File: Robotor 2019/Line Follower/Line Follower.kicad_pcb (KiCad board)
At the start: 2 copper layers, 3.7 x 3.6 mm, 96 parts, among them J1 Conn_01x03_Male, J2 Conn_01x04_Female, J3 USB_B_Mini, J4 Conn_01x03_Female, J5 Conn_01x03_Female, J7 Conn_01x03_Female, J8 Conn_01x03_Female, M1 Motor_DC, M2 Motor_DC, U1 AMS1117-3V3, U10 ITR8307, U11 ITR8307, U12 ITR8307, U13 ITR8307, U14 ITR8307, U15 ITR8307, U3 AMS1117-5.0, U4 STM32F103C8Tx, U5 ITR8307, U6 L298P, U7 ITR8307, U8 ITR8307, U9 ITR8307, Y1 32.768Khz, Y2 8Mhz

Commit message: Line Follower robot electric schematic and PCB.
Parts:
- added REF**: MountingHole_2.5mm, MountingHole:MountingHole_2.5mm, B.Cu at (55.6, 42.0)
- added REF**: MountingHole_2.5mm, MountingHole:MountingHole_2.5mm, B.Cu at (40.6, 42.2)
- added REF**: MountingHole_2.5mm, MountingHole:MountingHole_2.5mm, F.Cu at (55.6, 168.8)
- added REF**: MountingHole_2.5mm, MountingHole:MountingHole_2.5mm, F.Cu at (40.6, 168.7)
- added REF**: MountingHole_2.5mm, MountingHole:MountingHole_2.5mm, F.Cu at (248.9, 46.0)
- added REF**: MountingHole_2.5mm, MountingHole:MountingHole_2.5mm, F.Cu at (224.5, 46.0)
- added REF**: MountingHole_2.5mm, MountingHole:MountingHole_2.5mm, B.Cu at (248.9, 164.8)
- added REF**: MountingHole_2.5mm, MountingHole:MountingHole_2.5mm, B.Cu at (224.5, 164.8)
- added SW1: SW_Push, Button_Switch_SMD:SW_Push_1P1T_NO_6x6mm_H9.5mm, F.Cu at (117.0, 122.3)
- C15, C16, C17, C18, C19, C20, C21, C22, C23, C24, J3, R10, R11, R12, R14, R16, R18, R22, R24, R26, R28, R3, R30, R32, R9, U10, U11, U12, U13, U14, U15, U5, U7, U8, U9: moved to B.Cu
- R13, R15, R17, R19, R21, R23, R25, R27, R29, R31: footprint Resistor_SMD:R_0805_2012Metric_Pad1.15x1.40mm_HandSolder -> Resistor_SMD:R_1206_3216Metric_Pad1.42x1.75mm_HandSolder; moved to B.Cu
- moved J7 229.0 mm to (254.0, 146.1)
- moved J3 224.8 mm to (256.0, 104.4), turned to 270 degrees
- moved J8 210.1 mm to (221.7, 146.9)
- moved J1 194.1 mm to (157.0, 163.3), turned to 270 degrees
- moved D7 190.2 mm to (187.7, 172.0), turned to 180 degrees
- moved J4 187.0 mm to (254.0, 66.5), turned to 180 degrees
- moved R5 184.4 mm to (255.0, 137.7), turned to 180 degrees
- moved R10 182.2 mm to (242.1, 103.9), turned to 90 degrees
- moved D8 179.1 mm to (182.6, 165.1)
- moved M2 177.2 mm to (183.9, 149.1), turned to 270 degrees
- moved R33 176.9 mm to (256.0, 54.6)
- moved D5 171.7 mm to (168.7, 171.2)
- moved D6 171.5 mm to (173.7, 165.1), turned to 180 degrees
- moved R9 171.3 mm to (244.9, 97.5), turned to 180 degrees
- moved U1 169.4 mm to (133.3, 185.8), turned to 180 degrees
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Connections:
- net US3_IN renamed Net-(U4-Pad45)
- net US3_OUT renamed Net-(U4-Pad46)
- C15 pad 1: +5V -> +3V3
- C16 pad 1: +5V -> +3V3
- C17 pad 1: +5V -> +3V3
- C18 pad 1: +5V -> +3V3
- C19 pad 1: +5V -> +3V3
- C20 pad 1: +5V -> +3V3
- C21 pad 1: +5V -> +3V3
- C22 pad 1: +5V -> +3V3
- C23 pad 1: +5V -> +3V3
- C24 pad 1: +5V -> +3V3
- R12 pad 1: +5V -> +3V3
- R13 pad 1: S7 -> S1
- R14 pad 1: +5V -> +3V3
- R15 pad 1: S8 -> S2
- R16 pad 1: +5V -> +3V3
- R17 pad 1: S9 -> S3
- R18 pad 1: +5V -> +3V3
- R19 pad 1: S10 -> S4
- R21 pad 1: S6 -> S8
- R22 pad 1: +5V -> +3V3
- R23 pad 1: S5 -> S7
- R24 pad 1: +5V -> +3V3
- R25 pad 1: S4 -> S6
- R26 pad 1: +5V -> +3V3
- R27 pad 1: S3 -> S5
- R28 pad 1: +5V -> +3V3
- R29 pad 1: S2 -> S10
- R30 pad 1: +5V -> +3V3
- R31 pad 1: S1 -> S9
- R32 pad 1: +5V -> +3V3
- U4 pad 10: S1 -> S3
- U4 pad 12: S3 -> S1
- U4 pad 14: S5 -> S8
- U4 pad 15: S6 -> S7
- U4 pad 16: S7 -> S6
- U4 pad 17: S8 -> S5
- U4 pad 18: S9 -> S10
- U4 pad 19: S10 -> S9
- U4 pad 21: H4 -> Net-(U4-Pad21)
- U4 pad 22: H3 -> Net-(U4-Pad22)
- U4 pad 25: US1_IN -> H1
- U4 pad 26: US1_OUT -> H2
- U4 pad 27: US2_IN -> H3
- U4 pad 28: US2_OUT -> H4
- U4 pad 30: EnA -> Net-(U4-Pad30)
- U4 pad 31: EnB -> Net-(U4-Pad31)
- U4 pad 39: M2IN1 -> EnB
- U4 pad 40: M1IN2 -> M2IN1
- U4 pad 41: M1IN1 -> EnA
- U4 pad 42: H2 -> M1IN2
- U4 pad 43: H1 -> M1IN1
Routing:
- net +3V3: track 0.00 -> 1078.7 mm, vias 0 -> 2
- net +7.5V: track 0.00 -> 471.6 mm
- net +5V: track 0.00 -> 286.5 mm
- net Net-(D3-Pad2): track 0.00 -> 189.9 mm
- net Net-(D1-Pad2): track 0.00 -> 185.8 mm
- net S9: track 0.00 -> 177.2 mm, vias 0 -> 1
- net S10: track 0.00 -> 166.5 mm, vias 0 -> 1
- net H3: track 0.00 -> 154.8 mm, vias 0 -> 1
- net S1: track 0.00 -> 153.0 mm, vias 0 -> 1
- net S5: track 0.00 -> 152.8 mm, vias 0 -> 1
- net H2: track 0.00 -> 150.0 mm, vias 0 -> 1
- net Net-(D5-Pad2): track 0.00 -> 148.5 mm
- net S2: track 0.00 -> 140.6 mm, vias 0 -> 1
- net Net-(D7-Pad2): track 0.00 -> 140.4 mm
- net S6: track 0.00 -> 135.7 mm, vias 0 -> 1
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- added copper zone on B.Cu, net GND
- added copper zone on F.Cu, net GND
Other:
- board size 3.7 x 3.6 mm -> 239.3 x 180.3 mm

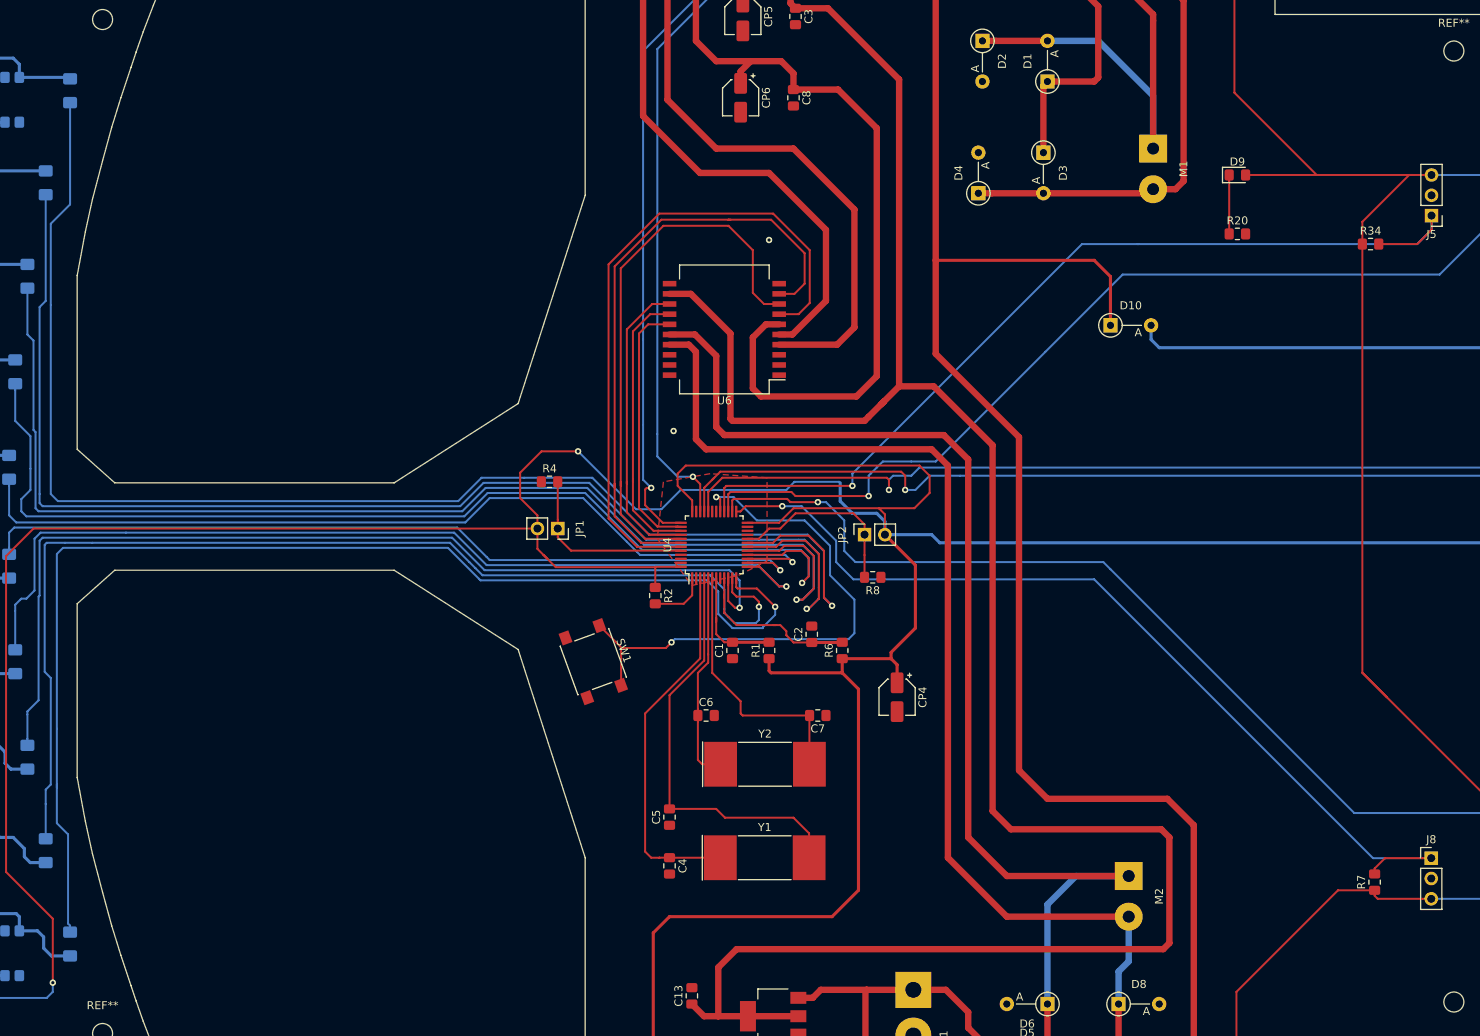
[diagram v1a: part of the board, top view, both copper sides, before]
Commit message: Small tweaks to vias, paths, added parts lists.
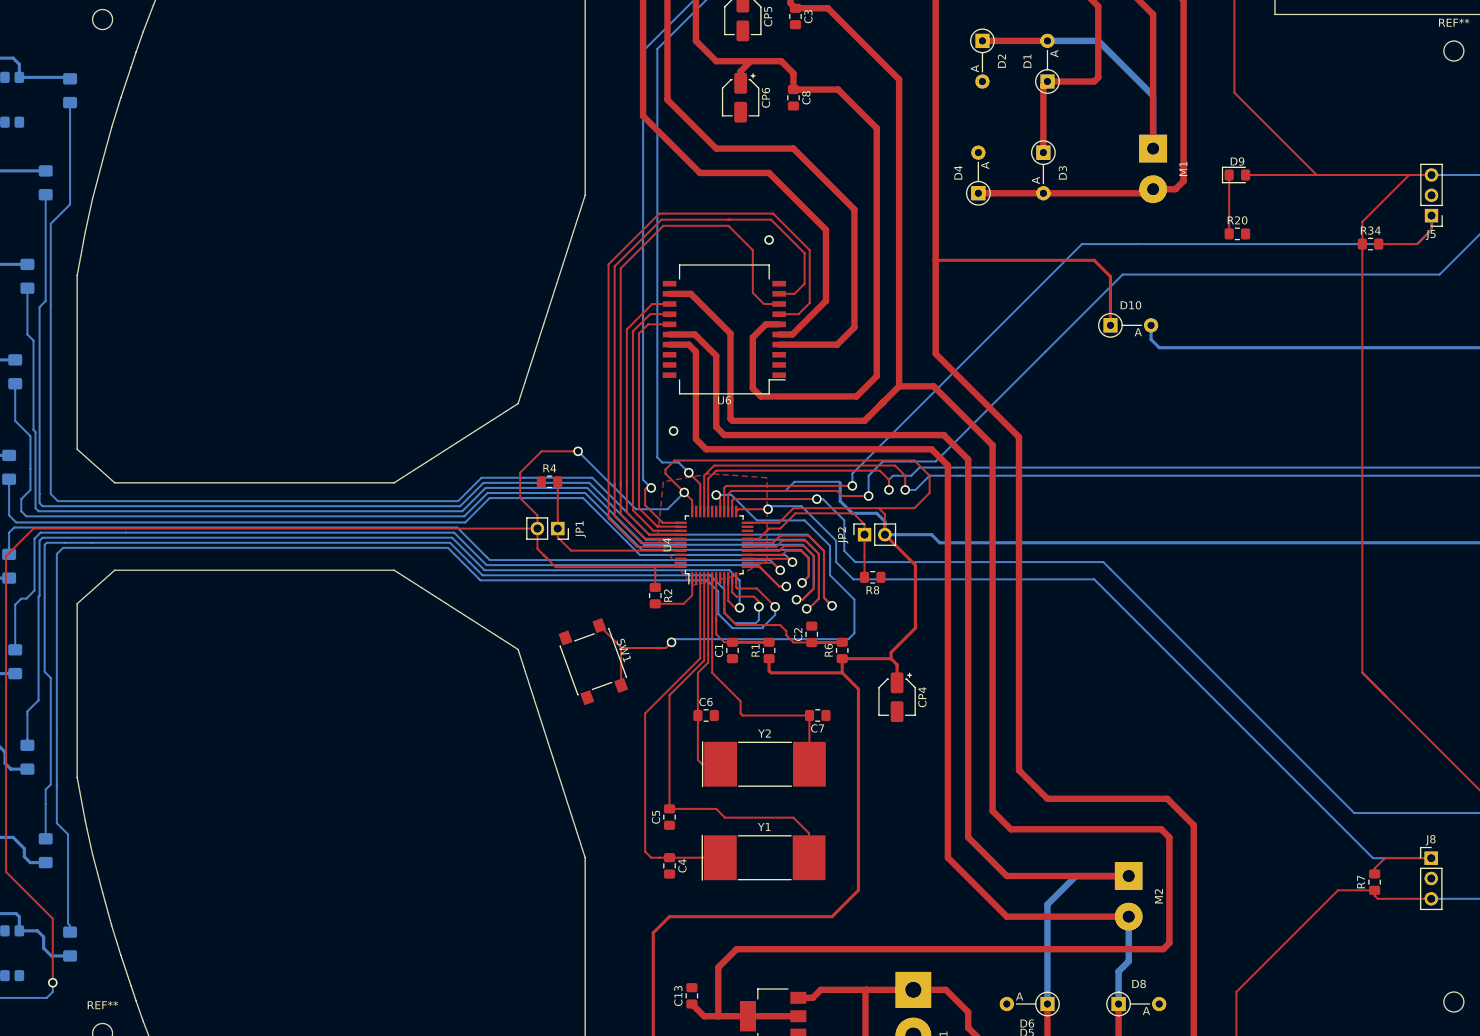
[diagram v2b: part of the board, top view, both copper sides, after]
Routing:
- net +3V3: track 1078.7 -> 1068.7 mm, vias 2 -> 3
- net PA11: track 119.2 -> 120.9 mm
- net PA12: track 120.5 -> 121.7 mm

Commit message: no message
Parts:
- removed the REF** at (248.9, 164.8)
- removed the REF** at (224.5, 164.8)
- added REF**: MountingHole_2.5mm, MountingHole:MountingHole_2.5mm, B.Cu at (224.5, 158.4)
- added REF**: MountingHole_2.5mm, MountingHole:MountingHole_2.5mm, B.Cu at (248.9, 158.4)
- moved C17 30.0 mm to (65.3, 143.6)
- moved C23 30.0 mm to (65.3, 60.3)
- moved R13 30.0 mm to (81.5, 157.6)
- moved R31 30.0 mm to (81.5, 50.9)
- moved C16 30.0 mm to (60.7, 108.1)
- moved C20 30.0 mm to (60.7, 95.9)
- moved C22 30.0 mm to (61.5, 83.9)
- moved R12 30.0 mm to (68.2, 160.5)
- moved R15 30.0 mm to (78.5, 145.9)
- moved R16 30.0 mm to (62.9, 137.2)
- moved R17 30.0 mm to (76.2, 134.2)
- moved R18 30.0 mm to (61.3, 125.2)
- moved R19 30.0 mm to (74.7, 122.3)
- moved R21 30.0 mm to (73.9, 110.4)
- moved R22 30.0 mm to (60.6, 113.3)
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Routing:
- net +3V3: track 1068.7 -> 1011.4 mm
- net S8: track 106.1 -> 76.1 mm
- net S5: track 152.8 -> 122.8 mm
- net S1: track 153.0 -> 123.1 mm
- net S7: track 113.2 -> 83.2 mm
- net S6: track 135.7 -> 105.7 mm
- net S4: track 118.2 -> 88.2 mm
- net S3: track 124.1 -> 94.2 mm
- net S2: track 140.6 -> 110.6 mm
- net S9: track 177.2 -> 147.2 mm
- net S10: track 166.5 -> 136.5 mm
- net H2: track 150.0 -> 148.1 mm
- net H1: track 115.2 -> 114.2 mm
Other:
- board size 239.3 x 180.3 mm -> 209.3 x 180.3 mm
